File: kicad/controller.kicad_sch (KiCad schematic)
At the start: 30 parts, among them J10 JTAG, J11 I2C, J8 USB_B_Micro, J9 ESPFlash, Q3 S8050, Q4 S8050, SW3 RESET, SW4 BOOT, U5 CP2102N-A02-GQFN24, U6 ESP32-WROOM-32D

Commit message: cleanup
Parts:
- removed D5: BLUE, LED_SMD:LED_0603_1608Metric, symbol Device:LED
- removed J10: JTAG, Connector_PinHeader_2.54mm:PinHeader_2x05_P2.54mm_Vertical, symbol Connector_Generic:Conn_02x05_Counter_Clockwise
- removed J11: I2C, Connector_PinHeader_2.54mm:PinHeader_1x04_P2.54mm_Vertical, symbol Connector_Generic:Conn_01x04
- removed JP1: SolderJumper_3_Bridged123, SaawLib:SolderJumper-3_P1.3mm_Bridged123_Pad1.0x1.5mm_NumberLabels, symbol Jumper:SolderJumper_3_Bridged123
- removed R18: 10k, Resistor_SMD:R_0603_1608Metric, symbol Device:R
- removed R21: 1k, Resistor_SMD:R_0603_1608Metric, symbol Device:R
- removed SW3: RESET, Button_Switch_SMD:SW_Push_SPST_NO_Alps_SKRK, symbol Switch:SW_Push
- removed SW4: BOOT, Button_Switch_SMD:SW_Push_SPST_NO_Alps_SKRK, symbol Switch:SW_Push
- added C11: 10uF, Capacitor_SMD:C_0603_1608Metric, symbol Device:C_Small
- added D4: MBR120, Diode_SMD:D_SOD-123F, symbol Device:D_Schottky
- added JP3: I2C_PU, SaawLib:SolderJumper-3_P1.3mm_Bridged123_Pad1.0x1.5mm_NumberLabels, symbol Jumper:SolderJumper_3_Bridged123
- C10: renamed from C12; MPN (none) -> CL10A475KQ8NNWC
- C12: renamed from C13; MPN (none) -> CL10A106MA8NRNC
- C13: renamed from C14; MPN (none) -> CL10B104KB8NNWC
- C8: renamed from C15; MPN (none) -> CL10B105KA8NFNC
- C9: renamed from C11; MPN (none) -> CL10B104KB8NNWC
- D5: renamed from D6; MPN (none) -> 150060RS75000
- J6: renamed from J8; MPN (none) -> USB3076-30-A
- J7: renamed from J9; value ESPFlash -> PROG; footprint Connector_PinHeader_2.54mm:PinHeader_2x03_P2.54mm_Vertical -> Connector_IDC:IDC-Header_2x03_P2.54mm_Vertical
- Q3, Q4: value S8050 -> SS8050-G; MPN (none) -> SS8050-G
- R14: renamed from R22; MPN (none) -> RC0603FR-0710KL
- R15: renamed from R23; MPN (none) -> RC0603FR-0710KL
- R16: renamed from R13; value 22.1K -> 22.1k; MPN (none) -> RC0603FR-0722K1L
- R17: renamed from R16; value 47.5K -> 47.5k; MPN (none) -> RC0603FR-1047K5L
- R18: renamed from R17; value 1K -> 1k; MPN (none) -> RC0603FR-071KL
- R19: renamed from R14; MPN (none) -> RC0603FR-0710KL
- R20: renamed from R15; MPN (none) -> RC0603FR-0710KL
- R21: renamed from R19; value 2.2K -> 4.7k; MPN (none) -> RC0603FR-074K7L
- R22: renamed from R24; MPN (none) -> RC0603FR-071KL
- R23: renamed from R20; value 2.2K -> 4.7k; MPN (none) -> RC0603FR-074K7L
- U5: MPN (none) -> CP2102N-A02-GQFN24R
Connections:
- net GPIO18 is gone; now on net SCL: U6.30 (IO18)
- net GPIO19 is gone; now on net SDA: U6.31 (IO19)
- net GND: now also C11.2
- net SCL: no longer U6.36 (IO22)
- net SDA: no longer U6.33 (IO21)
- net VBUS: now also D4.2 (A)
- net at R23.1: now also JP3.3 (B)
- net at R21.1: now also JP3.1 (A)
- net +3V3 renamed +3.3V
- net +3.3V: now also C11.1, JP3.2 (C); no longer J7.2 (Pin_2)
- net GPIO16: no longer names the net of U6.27 (IO16)
- net GPIO17: no longer names the net of U6.28 (IO17)
- net GPIO25/DAC1 renamed GPIO25
- net GPIO26/DAC2 renamed GPIO26
- net GPIO32: no longer names the net of U6.8 (IO32)
- net GPIO34: no longer names the net of U6.6 (IO34)
- net GPIO35: no longer names the net of U6.7 (IO35)
- net GPIO36/S_VP renamed GPIO36
- net GPIO39/S_VN: no longer names the net of U6.5 (SENSOR_VN)
- net IO2: no longer names the net of U6.24 (IO2)
- net IO5: no longer names the net of U6.29 (IO5)
- net MTCK: no longer names the net of U6.16 (IO13)
- net MTDI: no longer names the net of U6.14 (IO12)
- net MTDO: no longer names the net of U6.23 (IO15)
- net MTMS: no longer names the net of U6.13 (IO14)
- net VBUSDIV renamed VBUS_DETECT
- new net +5V: D4.1 (K), J7.2 (Pin_2)
- new net GPIO22: U6.36 (IO22)
- no-connect marks 21 -> 30
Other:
- note added: "Boot Strapping Pins: IO 0,2,5,12,15 I2C: IO 21, 22 JTAG: IO12-15"
- note added: "ESP-Prog"
- note added: "ESP-Prog compatible (Use 5V jumper). Logic 3.3V Power 5V"
- note added: "From 5V->3.3V LDO"
- note added: "I2C Pullup"
- note added: "PWR LED"
- note added: "USB"
- note added: "USB to UART (Optional)"
- note removed: "2x3 IDC 1.27mm"
- note removed: "2x5 IDC 1.27mm"
- note removed: "Boot Strapping Pins: IO 0,2,5,12,15 LED: IO2 I2C: IO 21, 22 JTAG: IO12-15"
- note removed: "Buttons"
- note removed: "Connectors"
- note removed: "I2C Pull-Up"
- note removed: "JTAG IO12-15"
- note removed: "Status / Pulldown"
- note removed: "USB to UART"
- company: (none) -> saawsm
- moved on the sheet: C10, C12, C13, C8, C9, D5, J6, J7, Q3, Q4, R14, R15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

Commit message: add pcb
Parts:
- removed C12: 10uF, Capacitor_SMD:C_0603_1608Metric, symbol Device:C_Small
- removed C8: 1uF, Capacitor_SMD:C_0603_1608Metric, symbol Device:C_Small
- added C13, C14, C15: 100nF, Capacitor_SMD:C_0603_1608Metric, symbol Device:C_Small
- added JP4: UART_TXD, Jumper:SolderJumper-2_P1.3mm_Open_RoundedPad1.0x1.5mm, symbol Jumper:SolderJumper_2_Open
- added JP5: UART_RXD, Jumper:SolderJumper-2_P1.3mm_Open_RoundedPad1.0x1.5mm, symbol Jumper:SolderJumper_2_Open
- C10: LCSC (none) -> C3849923; MOUSER (none) -> 187-CL10A475KQ8NNWC
- C11: value 10uF -> 22uF; LCSC (none) -> C96446; MOUSER (none) -> 187-CL10A106MA8NRNC
- C12: renamed from C13; LCSC (none) -> C1591; MOUSER (none) -> 187-CL10B104KB8NNNC
- C9: LCSC (none) -> C1591; MOUSER (none) -> 187-CL10B104KB8NNNC
- D4: value MBR120 -> SS24FL; LCSC (none) -> C894433; MOUSER (none) -> 512-SS24FL; MPN MBR120ESFT1G -> SS24FL
- D5: MOUSER (none) -> 710-150060RS75000
- J6: MOUSER (none) -> 640-USB3076-30-A
- JP3: now left out of the parts list
- Q3, Q4: LCSC (none) -> C164886; MOUSER (none) -> 750-SS8050-G
- R13: renamed from R16; LCSC (none) -> C137768; MOUSER (none) -> 603-RC0603FR-0722K1L
- R14: renamed from R17; LCSC (none) -> C4149630; MOUSER (none) -> 603-RC0603FR-1047K5L
- R15: renamed from R19; LCSC (none) -> C98220; MOUSER (none) -> 603-RC0603FR-0710KL
- R16: renamed from R20; LCSC (none) -> C98220; MOUSER (none) -> 603-RC0603FR-0710KL
- R17: renamed from R18; LCSC (none) -> C22548; MOUSER (none) -> 603-RC0603FR-071KL
- R18: renamed from R15; LCSC (none) -> C98220; MOUSER (none) -> 603-RC0603FR-0710KL
- R19: renamed from R14; LCSC (none) -> C98220; MOUSER (none) -> 603-RC0603FR-0710KL
- R20: renamed from R21; LCSC (none) -> C99782; MOUSER (none) -> 603-RC0603FR-074K7L
- R21: renamed from R22; LCSC (none) -> C22548; MOUSER (none) -> 603-RC0603FR-071KL
- R22: renamed from R23; LCSC (none) -> C99782; MOUSER (none) -> 603-RC0603FR-074K7L
- U5: LCSC (none) -> C969151; MOUSER (none) -> 634-CP2102NA02QFN24R
- U6: value ESP32-WROOM-32D -> ESP32-WROOM-32E; LCSC (none) -> C701343; MOUSER (none) -> 356-ESP32WRM32E128PH; MPN (none) -> ESP32-WROOM-32E-N16
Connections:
- net EN: now also C13.1
- net GND: now also C13.2, C14.2, C15.2
- net RXD: now also JP4.2 (B); no longer U5.21 (TXD)
- net TXD: now also JP5.2 (B); no longer U5.20 (RXD)
- net GPIO34: now reaches U6.6 (IO34)
- net GPIO34: now also C15.1
- net GPIO35: now reaches U6.7 (IO35)
- net GPIO35: now also C14.1
- net GPIO23: no longer names the net of U6.37 (IO23)
- net GPIO36: no longer names the net of U6.4 (SENSOR_VP)
- net VBUS: no longer names the net of D4.2 (A), J6.1 (VBUS), R13.1
- new net: JP5.1 (A), U5.20 (RXD)
- new net: JP4.1 (A), U5.21 (TXD)
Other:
- note added: "Auto Program DTR RTS EN IO0 1 1 1 1 0 0 1 1 1 0 0 1 0 1 1 0"
- note added: "ESP-Prog compatible (Use 5V jumper). See USB-UART solder jumpers Logic 3.3V Power 5V"
- note added: "Solder jumpers to use USB to UART"
- note removed: "Auto Program DTR RTS EN IO0 1 1 1 1 0 0 1 1 1 0 0 1 0 1 1 0 Alt. MMBT2222 ??"
- note removed: "Auto Reset"
- note removed: "ESP-Prog compatible (Use 5V jumper). Logic 3.3V Power 5V"
- note removed: "From 5V->3.3V LDO"
- note removed: "USB"
- title: Blugasm: Controller -> Blugasm
- moved on the sheet: C10, C11, C12, C9, D4, J6, Q3, Q4, R13, R14, R15, R16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

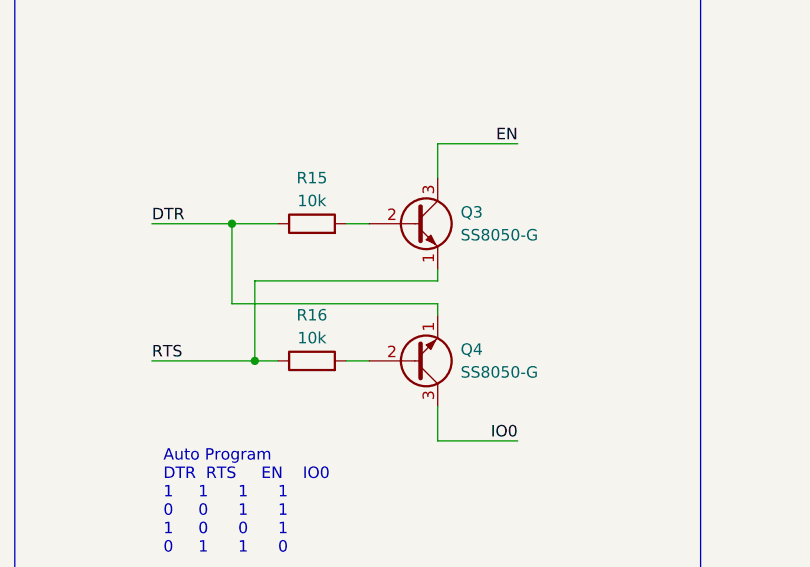
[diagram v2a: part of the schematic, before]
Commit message: fix incorrect footprint
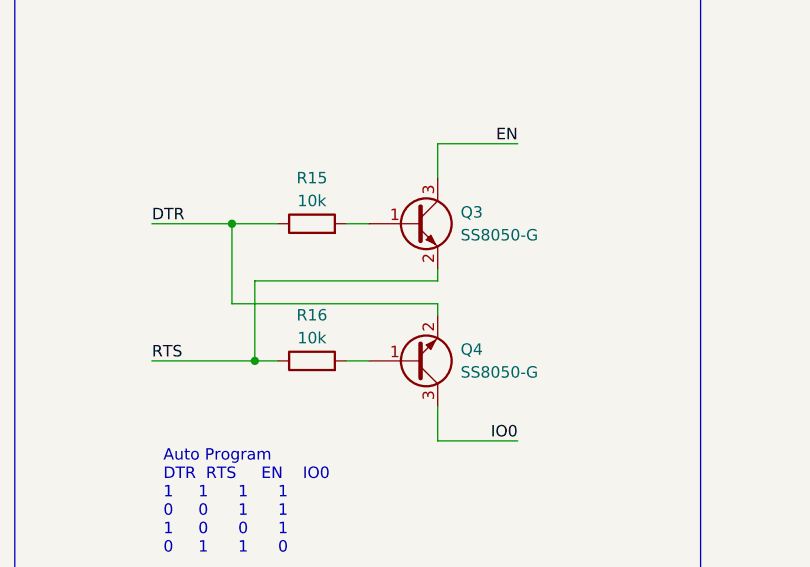
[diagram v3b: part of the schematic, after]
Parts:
- Q3, Q4: symbol Transistor_BJT:S8050 -> Device:Q_NPN_BEC
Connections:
- net DTR: now also Q4.2 (E); no longer Q4.1 (E)
- net RTS: now also Q3.2 (E); no longer Q3.1 (E)
- net at R16.2: now also Q4.1 (B); no longer Q4.2 (B)
- net at R15.2: now also Q3.1 (B); no longer Q3.2 (B)
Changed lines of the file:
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@@
   (title_block
     (title "Blugasm")
-    (date "2023-01-17")
+    (date "2023-01-24")
     (rev "1")
     (company "saawsm")
@@
     (pin "2")
   )
-  (symbol (lib_id "Transistor_BJT:S8050") (at 101.6 165.1 0) (mirror x) (unit 1)
+  (symbol (lib_id "Device:Q_NPN_BEC") (at 101.6 165.1 0) (mirror x) (unit 1)
     (in_bom yes) (on_board yes) (fields_autoplaced)
     (property "Reference" "Q4" (id 0) (at 106.68 163.8299 0)
@@
       (effects (font (size 1.27 1.27) italic) (justify left) hide)
     )
-    (property "Datasheet" "http://www.unisonic.com.tw/datasheet/S8050.pdf" (id 3) (at 101.6 165.1 0)
+    (property "Datasheet" "https://mouser.com/datasheet/2/80/SS8050_G_RevA181526-2506539.pdf" (id 3) (at 101.6 165.1 0)
       (effects (font (size 1.27 1.27)) (justify left) hide)
     )
@@
     (pin "1")
   )
-  (symbol (lib_id "Transistor_BJT:S8050") (at 101.6 149.86 0) (unit 1)
+  (symbol (lib_id "Device:Q_NPN_BEC") (at 101.6 149.86 0) (unit 1)
     (in_bom yes) (on_board yes) (fields_autoplaced)
     (property "Reference" "Q3" (id 0) (at 106.68 148.5899 0)
@@
       (effects (font (size 1.27 1.27) italic) (justify left) hide)
     )
-    (property "Datasheet" "http://www.unisonic.com.tw/datasheet/S8050.pdf" (id 3) (at 101.6 149.86 0)
+    (property "Datasheet" "https://mouser.com/datasheet/2/80/SS8050_G_RevA181526-2506539.pdf" (id 3) (at 101.6 149.86 0)
       (effects (font (size 1.27 1.27)) (justify left) hide)
     )
